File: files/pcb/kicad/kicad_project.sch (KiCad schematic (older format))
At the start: 19 parts, among them IC1 ATMEGA328-A, P1 CONN_6, SW1 SW_PUSH, U15 MY_PIN52, U16 MY_PIN52, U17 MY_PIN52, U18 MY_PIN52, X1 12MHz

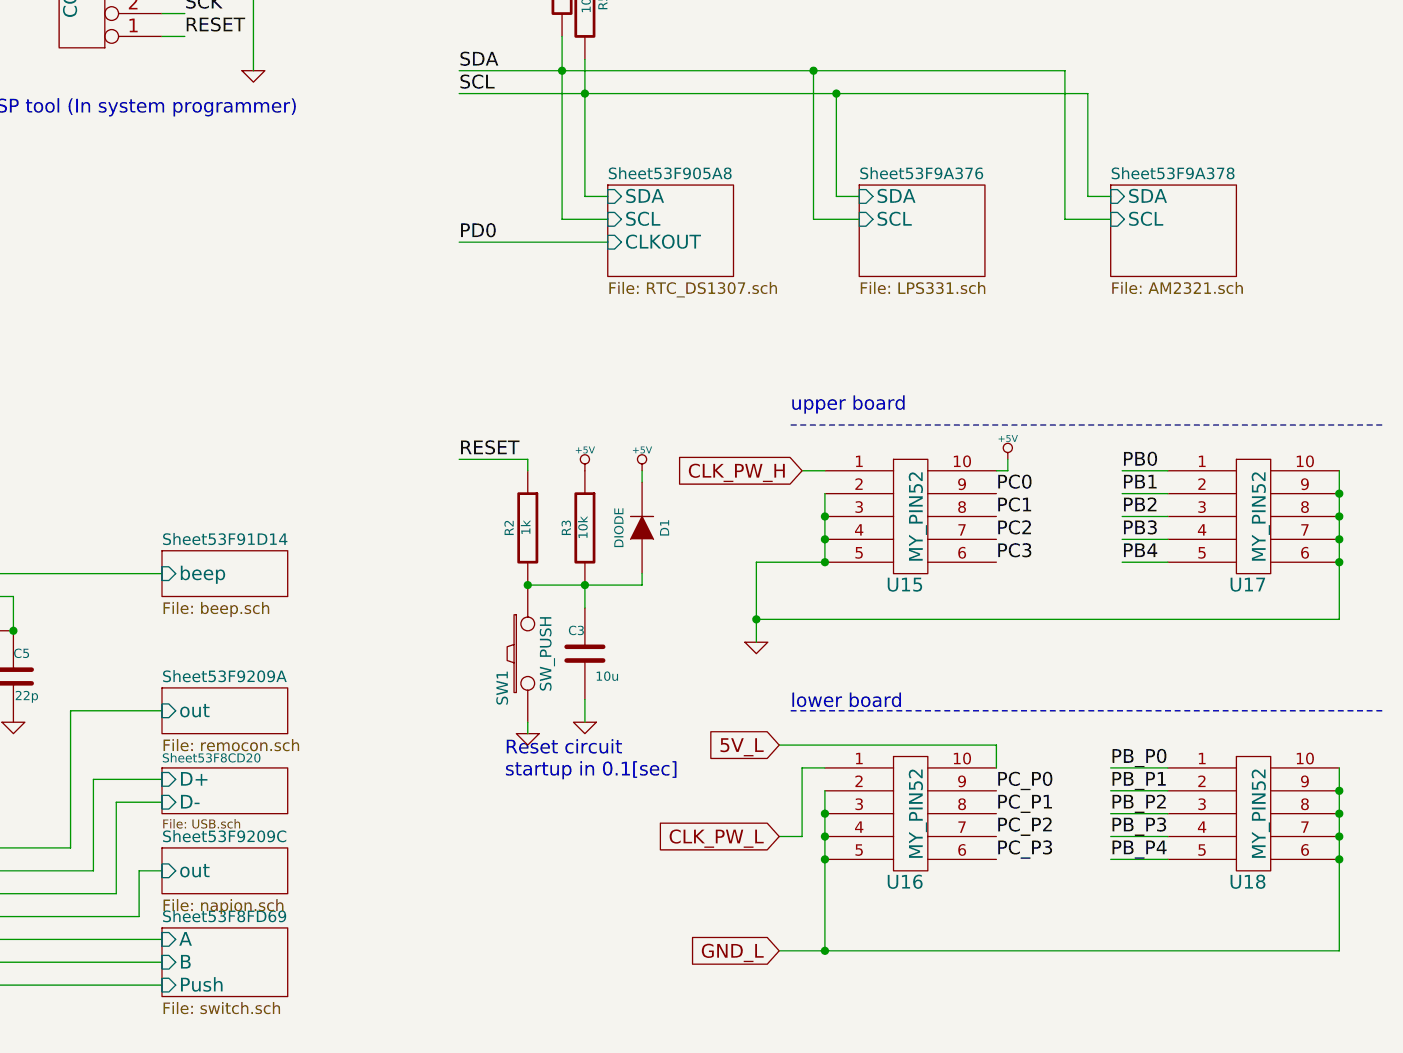
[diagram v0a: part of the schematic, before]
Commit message: 必要性の低い部品を削除
機能てんこ盛りよりシンプル小型化のほうがいいかなと思ったので一気に部品を削除
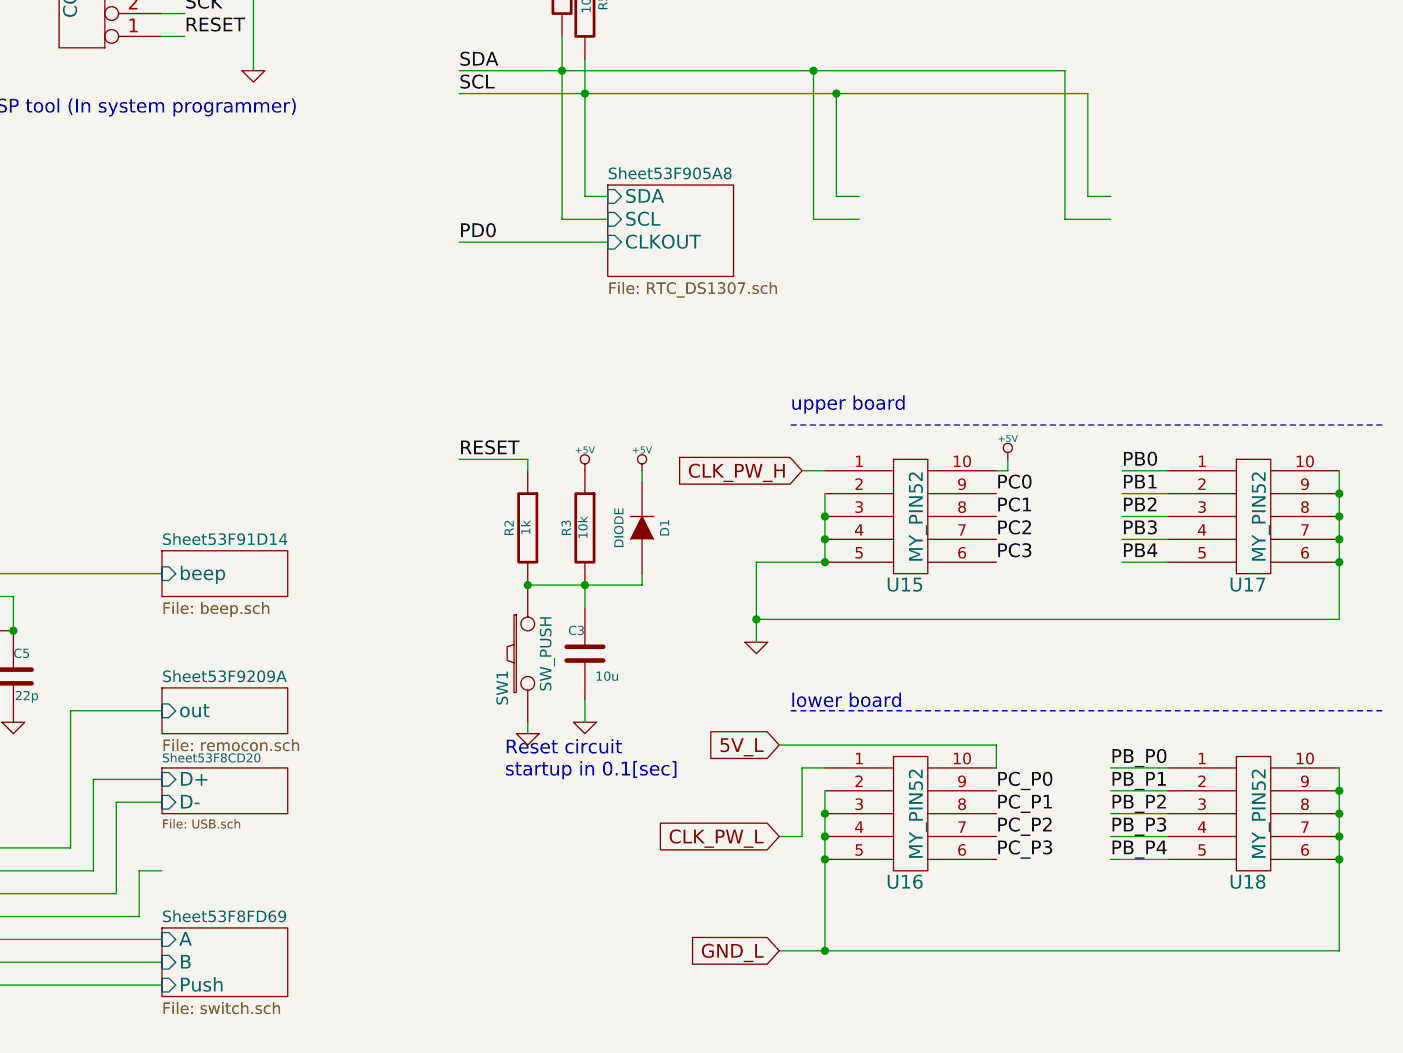
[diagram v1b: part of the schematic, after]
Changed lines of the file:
@@
 $Descr A4 11693 8268
 encoding utf-8
-Sheet 1 13
+Sheet 1 11
 Title ""
 Date "31 aug 2014"
@@
 F3 "SDA" I L 7700 3150 60
 F4 "SCL" I L 7700 3250 60
-$EndSheet
-$Sheet
-S 9900 3100 550  400
-U 53F9A379
-F0 "Sheet53F9A378" 50
-F1 "AM2321.sch" 50
-F2 "SDA" I L 9900 3150 60
-F3 "SCL" I L 9900 3250 60
 $EndSheet
 $Comp
@@
 Text Label 4450 4600 0    60   ~ 0
 MOSI
-$Sheet
-S 5750 6000 550  200
-U 53F9209D
-F0 "Sheet53F9209C" 50
-F1 "napion.sch" 50
-F2 "out" I L 5750 6100 60
-$EndSheet
 $Comp
 L C C4
@@
 Connection ~ 10900 4550
 Connection ~ 10900 4650
-$Sheet
-S 8800 3100 550  400
-U 53F9A377
-F0 "Sheet53F9A376" 50
-F1 "LPS331.sch" 50
-F2 "SDA" I L 8800 3150 60
-F3 "SCL" I L 8800 3250 60
-$EndSheet
 $EndSCHEMATC

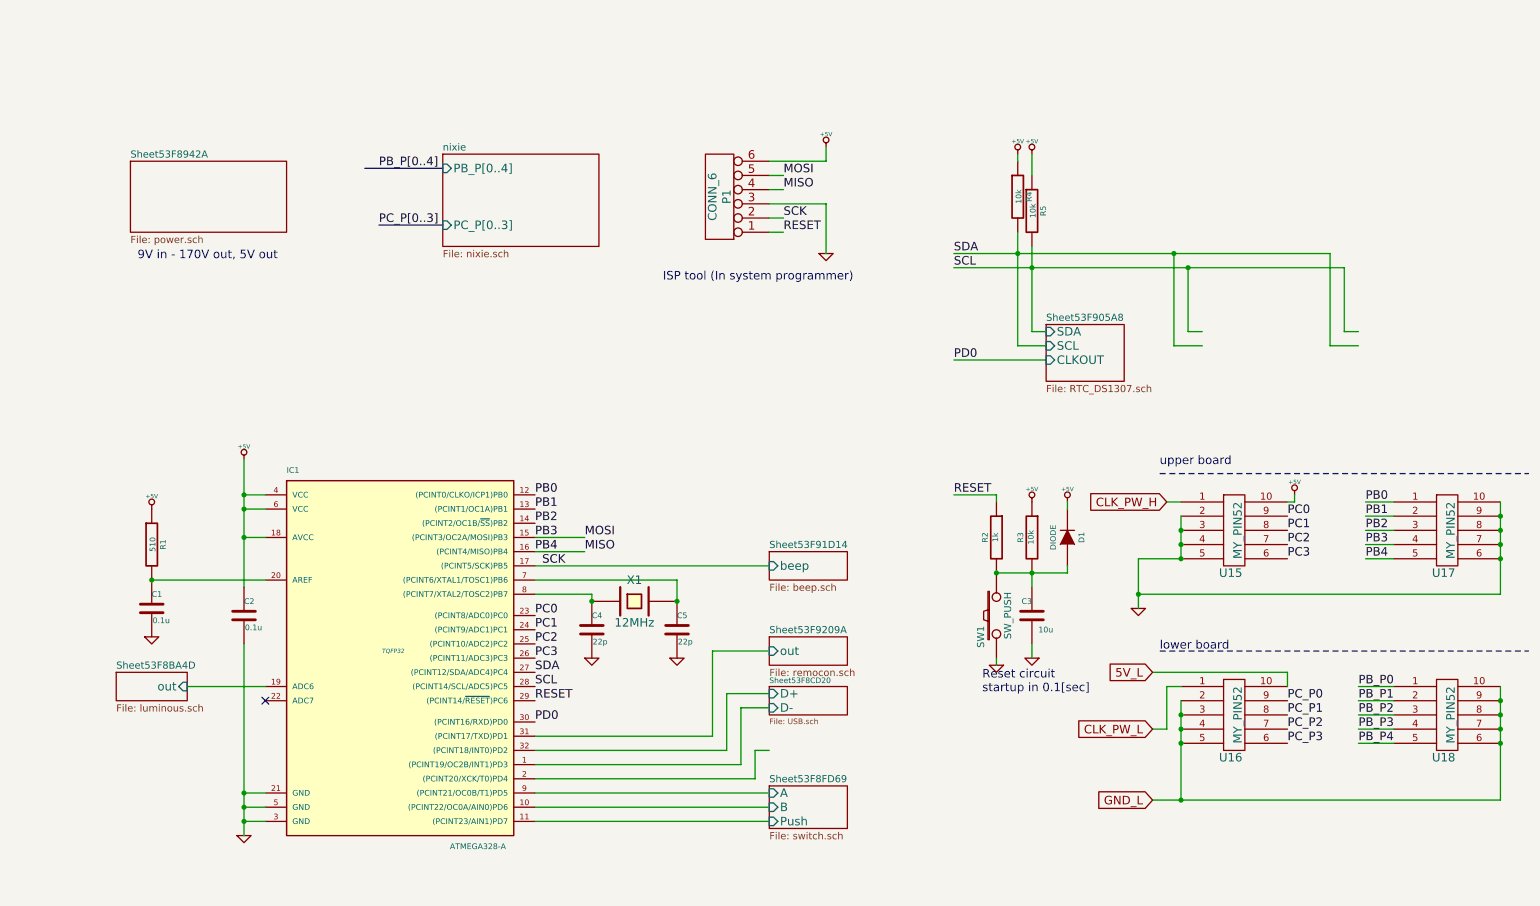
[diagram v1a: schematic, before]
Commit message: 設計見直し
部品見直し
USB・DCジャック自動切り替え
マイコンを下段のボードに移動
ニキシー管駆動電源を上段ボードに移動
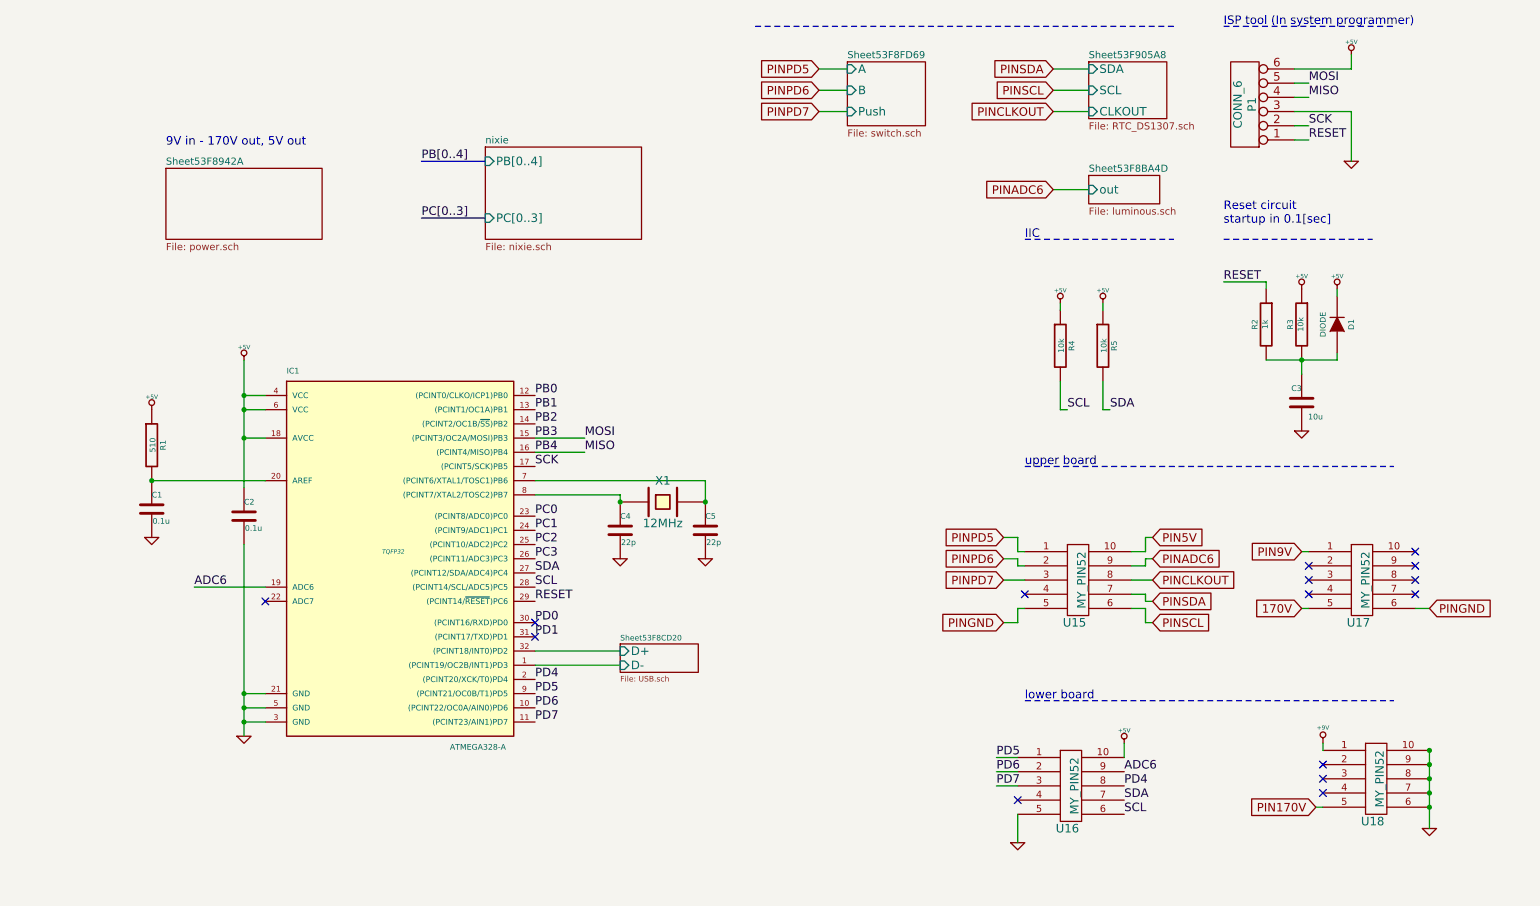
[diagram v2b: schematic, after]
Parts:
- removed SW1: SW_PUSH, ~, symbol SW_PUSH
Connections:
- net labels added: +9V, 170V, ADC6, PB[0..4], PC[0..3], PD1, PD4, PD5, PD6, PD7, PIN170V, PIN5V, PIN9V, PINADC6, PINCLKOUT, PINGND, PINPD5, PINPD6, PINPD7, PINSCL, PINSDA
- net labels removed: 5V_L, CLK_PW_H, CLK_PW_L, GND_L, PB_P0, PB_P1, PB_P2, PB_P3, PB_P4, PB_P[0..4], PC_P0, PC_P1, PC_P2, PC_P3, PC_P[0..3]
- wire segments 92 -> 80
- no-connect marks 1 -> 15
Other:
- note added: "IIC"
- moved on the sheet: C1, C2, C3, C4, C5, D1, IC1, P1, R1, R2, R3, R4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

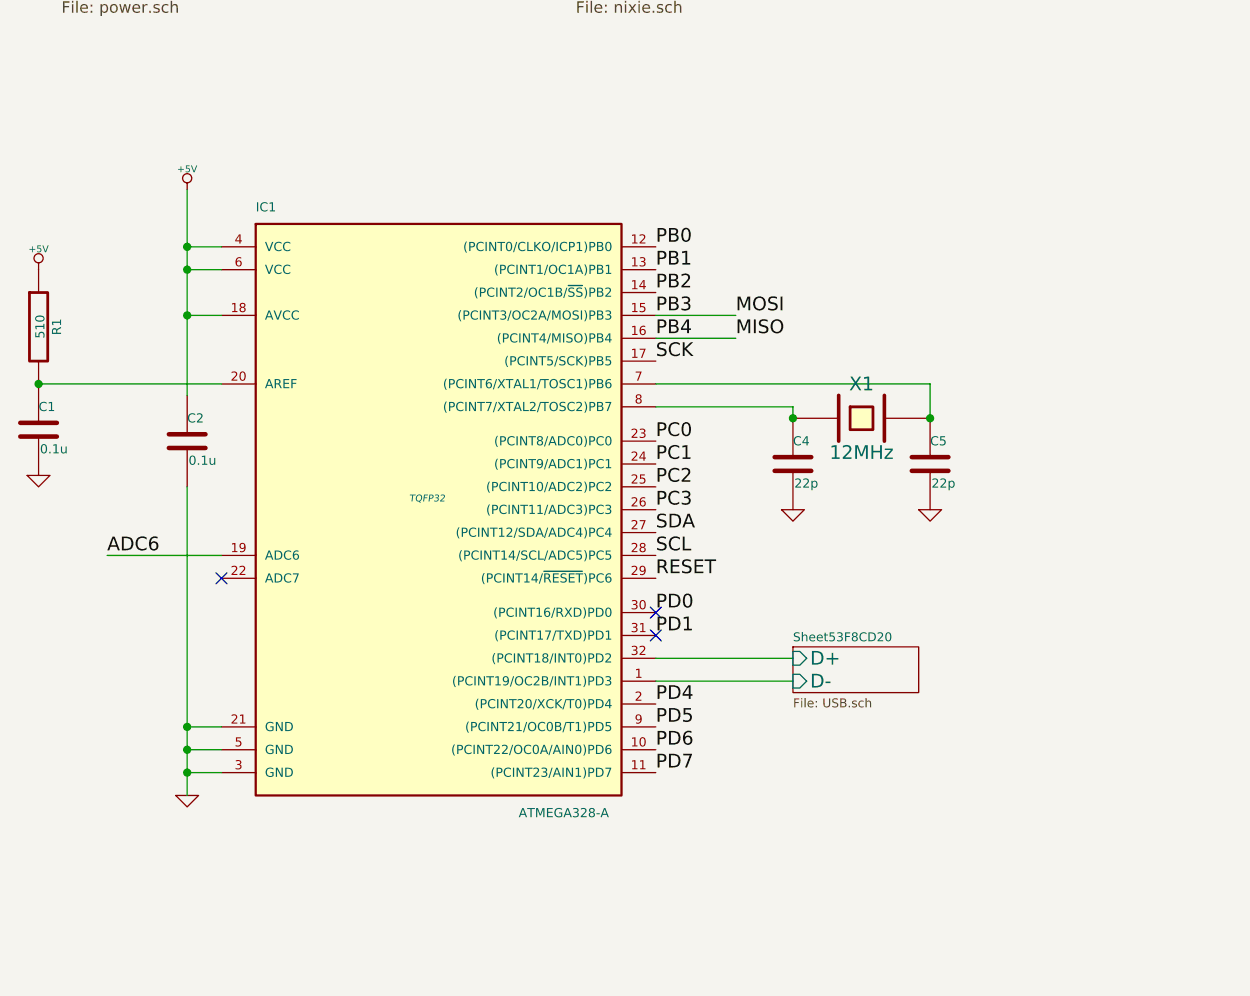
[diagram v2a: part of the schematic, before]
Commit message: PCB更新
ニキシー管の足を接続
電源仮接続
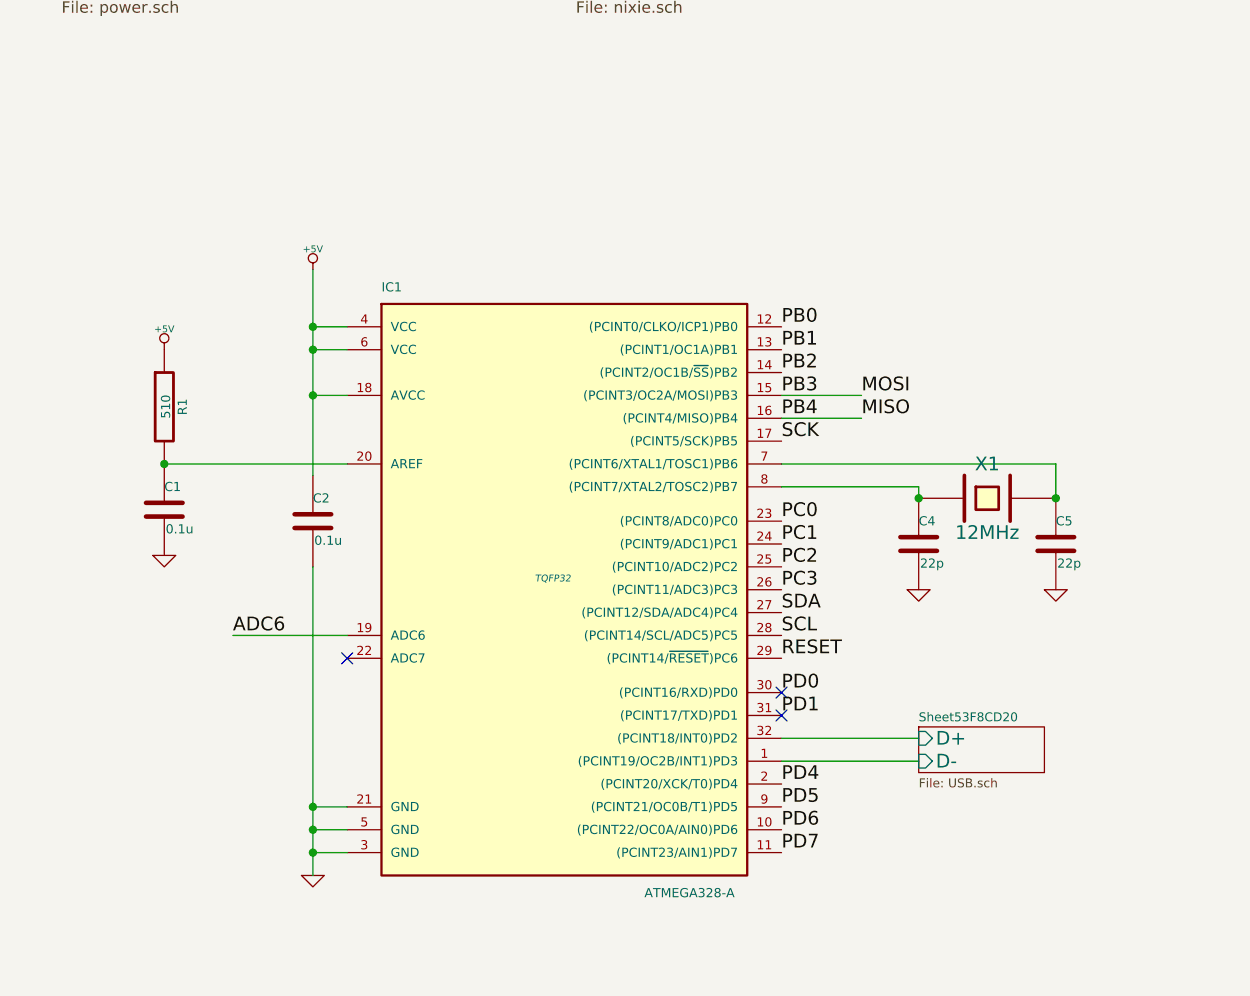
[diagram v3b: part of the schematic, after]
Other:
- moved on the sheet: C1, C2, C4, C5, IC1, R1, X1
